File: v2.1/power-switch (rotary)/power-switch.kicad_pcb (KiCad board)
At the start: 2 copper layers, 19 x 12.4 mm, 8 parts

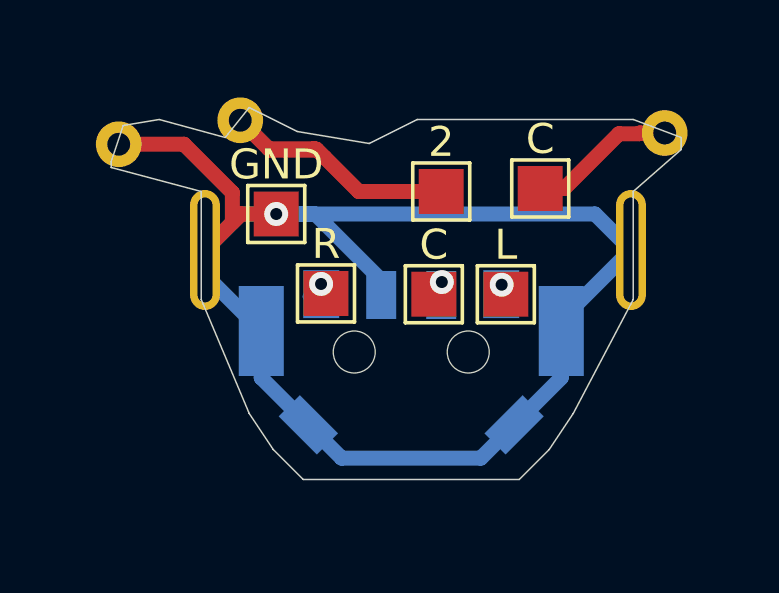
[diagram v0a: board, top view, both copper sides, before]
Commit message: cleanup
cleaned up readme, board files, added renders, made small tweaks to some of the boards (added identifiers and changed labels for consistency)
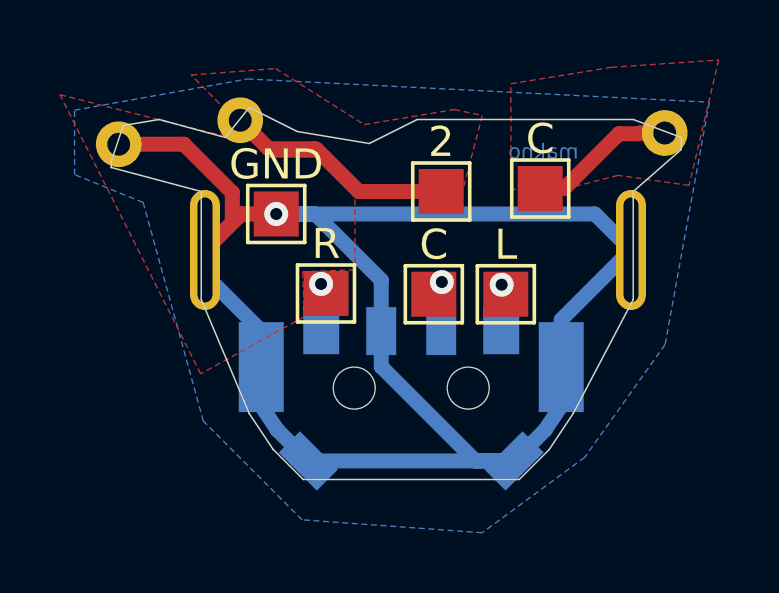
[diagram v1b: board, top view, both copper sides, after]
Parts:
- moved TM-2023 1.20 mm to (109.0, 74.8)
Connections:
- 2 pad 1: (no net) -> VDD
- C pad 1: (no net) -> VCC
- GND pad 1: (no net) -> GND
- Ref** pad 1: (no net) -> VCC
- Ref** pad 2: (no net) -> VDD
- Ref** pad 3: (no net) -> GND
- TM-2023 pad 6: (no net) -> GND
- TM-2023 pad GND: (no net) -> GND
- TM-2023 pad T: (no net) -> GND
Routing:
- net (no net): track 82.7 -> 4.71 mm, vias 4 -> 3
- net GND: track 0.00 -> 70.4 mm, vias 0 -> 1
- net VDD: track 0.00 -> 10.7 mm
- net VCC: track 0.00 -> 9.69 mm
- added copper zone on B.Cu, net GND
- added copper zone on F.Cu, net GND
- added copper zone on F.Cu, net VCC
- added copper zone on F.Cu, net VDD
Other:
- board text added: "https://github.com /makhowastaken /Soft-Latching-Power-Button"
- board text added: "makho"
